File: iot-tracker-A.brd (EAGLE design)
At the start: 25.4 x 21.3 mm, 23 parts, among them U1 ESP-WROOM-02, U2 TPL5111DDCR, U3 MCP1640T-I_CHY

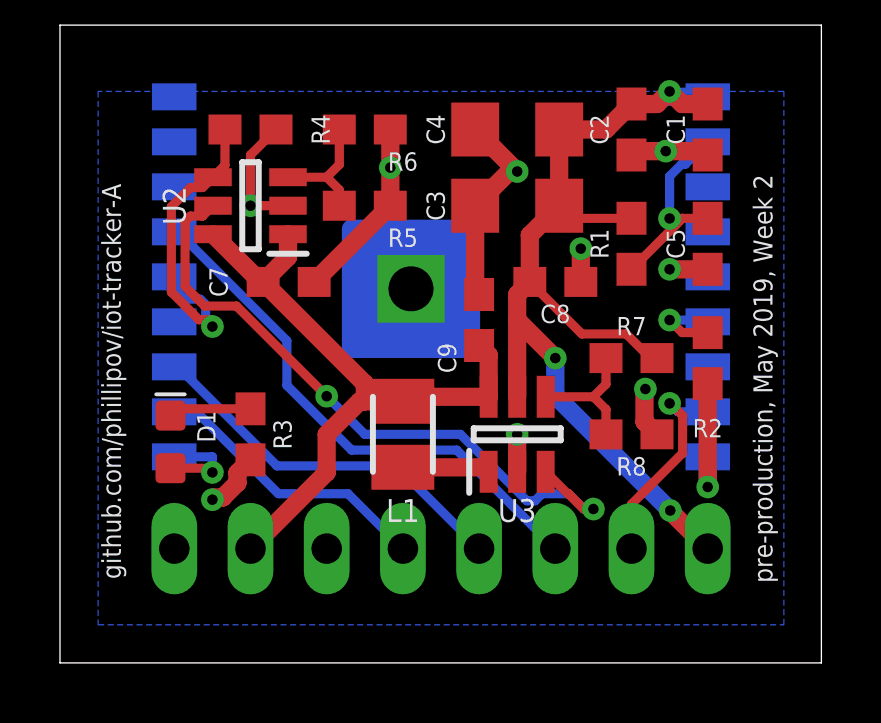
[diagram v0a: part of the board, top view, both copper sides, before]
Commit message: Moved pin headers to top layer and changed silkscreen fonts to vector
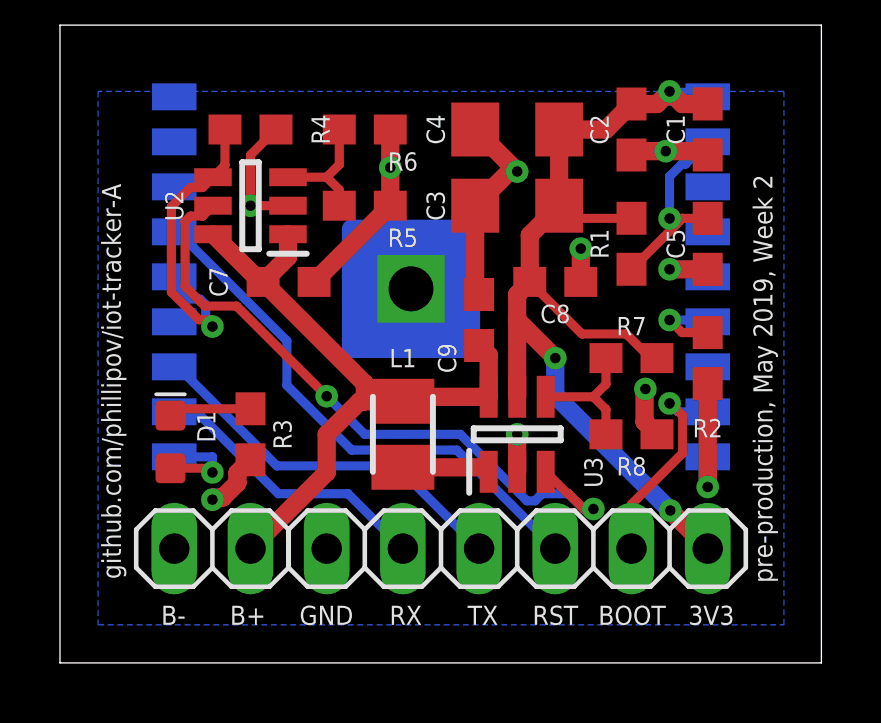
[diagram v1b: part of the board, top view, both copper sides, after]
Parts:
- flipped JP1 to the top, turned to 180 degrees
- flipped JP2 to the top, turned to 180 degrees
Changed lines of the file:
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@@
 <wire x1="25.38" y1="21.26" x2="0" y2="21.26" width="0" layer="20"/>
 <wire x1="0" y1="21.26" x2="0" y2="0" width="0" layer="20"/>
-<text x="6.731" y="1.27" size="0.635" layer="22" font="vector" rot="MR0">B+</text>
-<text x="4.064" y="1.27" size="0.635" layer="22" font="vector" rot="MR0">B-</text>
-<text x="9.652" y="1.27" size="0.635" layer="22" font="vector" rot="MR0">GND</text>
-<text x="14.478" y="1.27" size="0.635" layer="22" font="vector" rot="MR0">TX</text>
-<text x="11.938" y="1.27" size="0.635" layer="22" font="vector" rot="MR0">RX</text>
-<text x="17.145" y="1.27" size="0.635" layer="22" font="vector" rot="MR0">RST</text>
-<text x="20.066" y="1.27" size="0.635" layer="22" font="vector" rot="MR0">BOOT</text>
-<text x="22.352" y="1.27" size="0.635" layer="22" font="vector" rot="MR0">3V3</text>
+<text x="6.858" y="1.905" size="0.635" layer="21" font="vector" rot="R180">B+</text>
+<text x="4.191" y="1.905" size="0.635" layer="21" font="vector" rot="R180">B-</text>
+<text x="9.779" y="1.905" size="0.635" layer="21" font="vector" rot="R180">GND</text>
+<text x="14.605" y="1.905" size="0.635" layer="21" font="vector" rot="R180">TX</text>
+<text x="12.065" y="1.905" size="0.635" layer="21" font="vector" rot="R180">RX</text>
+<text x="17.272" y="1.905" size="0.635" layer="21" font="vector" rot="R180">RST</text>
+<text x="20.193" y="1.905" size="0.635" layer="21" font="vector" rot="R180">BOOT</text>
+<text x="22.479" y="1.905" size="0.635" layer="21" font="vector" rot="R180">3V3</text>
 <text x="2.032" y="2.794" size="0.635" layer="21" font="vector" rot="R90">github.com/phillipov/iot-tracker-A</text>
 <text x="23.749" y="2.667" size="0.635" layer="21" font="vector" rot="R90">pre-production, May 2019, Week 2</text>
@@
 <attribute name="MOUSER_PART_NUMBER" value="" x="49.53" y="40.64" size="1.778" layer="27" rot="R90" display="off"/>
 <attribute name="MOUSER_PRICE-STOCK" value="" x="49.53" y="40.64" size="1.778" layer="27" rot="R90" display="off"/>
-<attribute name="NAME" x="11.43" y="5.08" size="0.762" layer="25" rot="R180" align="center"/>
+<attribute name="NAME" x="11.43" y="10.16" size="0.6096" layer="25" font="vector" ratio="20" rot="R180" align="center"/>
 </element>
 <element name="R1" library="SparkFun-Resistors" library_urn="urn:adsk.eagle:library:532" package="0603" package3d_urn="urn:adsk.eagle:package:39650/1" value="10k" x="19.05" y="13.97" smashed="yes" rot="R270">
@@
 <attribute name="MANUFACTURER_PART_NUMBER" value="TPL5111DDCR" x="-13.97" y="45.72" size="1.778" layer="27" rot="R180" display="off"/>
 <attribute name="MOUSER_PART_NUMBER" value="" x="-13.97" y="45.72" size="1.778" layer="27" rot="R180" display="off"/>
-<attribute name="NAME" x="3.81" y="15.24" size="0.762" layer="25" rot="R270" align="center"/>
+<attribute name="NAME" x="3.81" y="15.24" size="0.6096" layer="25" font="vector" ratio="20" rot="R270" align="center"/>
 </element>
 <element name="U3" library="MCP1640T-I_CHY" package="SOT95P270X145-6N" value="MCP1640T-I_CHY" x="15.24" y="7.62" smashed="yes" rot="R90">
@@
 <attribute name="MOUSER_PART_NUMBER" value="579-MCP1640TI/CHY" x="40.64" y="39.37" size="1.778" layer="27" rot="R90" display="off"/>
 <attribute name="MOUSER_PRICE-STOCK" value="https://www.mouser.com/Search/Refine.aspx?Keyword=579-MCP1640TI%2FCHY" x="40.64" y="39.37" size="1.778" layer="27" rot="R90" display="off"/>
-<attribute name="NAME" x="15.24" y="5.08" size="0.762" layer="25" rot="R180" align="center"/>
-</element>
-<element name="JP1" library="pinhead" library_urn="urn:adsk.eagle:library:325" package="1X06" package3d_urn="urn:adsk.eagle:package:22472/2" value="" x="15.24" y="3.81" smashed="yes" rot="MR0">
-<attribute name="VALUE" x="22.86" y="0.635" size="1.27" layer="28" rot="MR0"/>
-</element>
-<element name="JP2" library="pinhead" library_urn="urn:adsk.eagle:library:325" package="1X02" package3d_urn="urn:adsk.eagle:package:22435/2" value="" x="5.08" y="3.81" smashed="yes" rot="MR0">
-<attribute name="VALUE" x="7.62" y="0.635" size="1.27" layer="28" rot="MR0"/>
+<attribute name="NAME" x="17.78" y="6.35" size="0.6096" layer="25" font="vector" ratio="20" rot="R90" align="center"/>
+</element>
+<element name="JP1" library="pinhead" library_urn="urn:adsk.eagle:library:325" package="1X06" package3d_urn="urn:adsk.eagle:package:22472/2" value="" x="15.24" y="3.81" smashed="yes" rot="R180">
+<attribute name="VALUE" x="22.86" y="6.985" size="1.27" layer="27" rot="R180"/>
+</element>
+<element name="JP2" library="pinhead" library_urn="urn:adsk.eagle:library:325" package="1X02" package3d_urn="urn:adsk.eagle:package:22435/2" value="" x="5.08" y="3.81" smashed="yes" rot="R180">
+<attribute name="VALUE" x="7.62" y="6.985" size="1.27" layer="27" rot="R180"/>
 </element>
 </elements>
@@
 <contactref element="U1" pad="11"/>
 <contactref element="JP1" pad="5"/>
-<wire x1="11.43" y1="3.81" x2="9.6012" y2="5.6388" width="0.3048" layer="16"/>
-<wire x1="9.6012" y1="5.6388" x2="7.2812" y2="5.6388" width="0.3048" layer="16"/>
+<wire x1="7.2812" y1="5.6388" x2="9.6012" y2="5.6388" width="0.3048" layer="16"/>
 <wire x1="7.2812" y1="5.6388" x2="4.55" y2="8.37" width="0.3048" layer="16"/>
 <wire x1="4.55" y1="8.37" x2="3.8075" y2="8.37" width="0.3048" layer="16"/>
+<wire x1="9.6012" y1="5.6388" x2="11.43" y2="3.81" width="0.3048" layer="16"/>
 </signal>
 <signal name="TX">
 <contactref element="U1" pad="12"/>
 <contactref element="JP1" pad="4"/>
-<wire x1="13.97" y1="3.81" x2="11.211990625" y2="6.568009375" width="0.3048" layer="16"/>
-<wire x1="11.211990625" y1="6.568009375" x2="7.23305" y2="6.568009375" width="0.3048" layer="16"/>
+<wire x1="7.23305" y1="6.568009375" x2="11.211990625" y2="6.568009375" width="0.3048" layer="16"/>
 <wire x1="7.23305" y1="6.568009375" x2="3.931059375" y2="9.87" width="0.3048" layer="16"/>
 <wire x1="3.931059375" y1="9.87" x2="3.8075" y2="9.87" width="0.3048" layer="16"/>
+<wire x1="11.211990625" y1="6.568009375" x2="13.97" y2="3.81" width="0.3048" layer="16"/>
 </signal>
 <signal name="BOOT">
@@
 <wire x1="20.32" y1="8.6506" x2="20.5458" y2="8.4248" width="0.3048" layer="1"/>
 <wire x1="20.5458" y1="8.4248" x2="20.57625" y2="8.4248" width="0.3048" layer="1"/>
-<wire x1="19.05" y1="5.28895" x2="19.05" y2="3.81" width="0.3048" layer="1"/>
-<wire x1="20.7548" y1="6.99375" x2="19.05" y2="5.28895" width="0.3048" layer="1"/>
+<wire x1="19.05" y1="5.28895" x2="20.7548" y2="6.99375" width="0.3048" layer="1"/>
+<wire x1="19.05" y1="3.81" x2="19.05" y2="5.28895" width="0.3048" layer="1"/>
 </signal>
 <signal name="EN">
@@
 <wire x1="17.3952" y1="10.9648" x2="18.87625" y2="10.9648" width="0.3048" layer="1"/>
 <wire x1="18.87625" y1="10.9648" x2="19.68105" y2="10.16" width="0.3048" layer="1"/>
-<wire x1="21.59" y1="3.81" x2="20.32" y2="5.08" width="0.6096" layer="1"/>
-<wire x1="20.32" y1="5.08" x2="20.3426" y2="5.08" width="0.6096" layer="1"/>
 <via x="20.3426" y="5.08" extent="1-16" drill="0.35"/>
 <wire x1="20.3426" y1="5.08" x2="16.51" y2="8.9126" width="0.6096" layer="16"/>
@@
 <via x="16.51" y="10.16" extent="1-16" drill="0.35"/>
 <wire x1="16.51" y1="10.16" x2="15.24" y2="11.43" width="0.6096" layer="1"/>
+<wire x1="20.3426" y1="5.08" x2="21.59" y2="3.8326" width="0.6096" layer="1"/>
+<wire x1="21.59" y1="3.8326" x2="21.59" y2="3.81" width="0.6096" layer="1"/>
 </signal>
 <signal name="V_BATT">
@@
 <contactref element="U1" pad="15"/>
 <contactref element="JP1" pad="3"/>
-<wire x1="16.51" y1="3.81" x2="13.225996875" y2="7.094003125" width="0.3048" layer="16"/>
 <wire x1="13.225996875" y1="7.094003125" x2="9.720078125" y2="7.094003125" width="0.3048" layer="16"/>
 <wire x1="9.720078125" y1="7.094003125" x2="7.5625" y2="9.25158125" width="0.3048" layer="16"/>
@@
 <wire x1="7.5625" y1="10.738559375" x2="3.931059375" y2="14.37" width="0.3048" layer="16"/>
 <wire x1="3.931059375" y1="14.37" x2="3.8075" y2="14.37" width="0.3048" layer="16"/>
+<wire x1="16.51" y1="3.81" x2="13.225996875" y2="7.094003125" width="0.3048" layer="16"/>
 </signal>
 </signals>

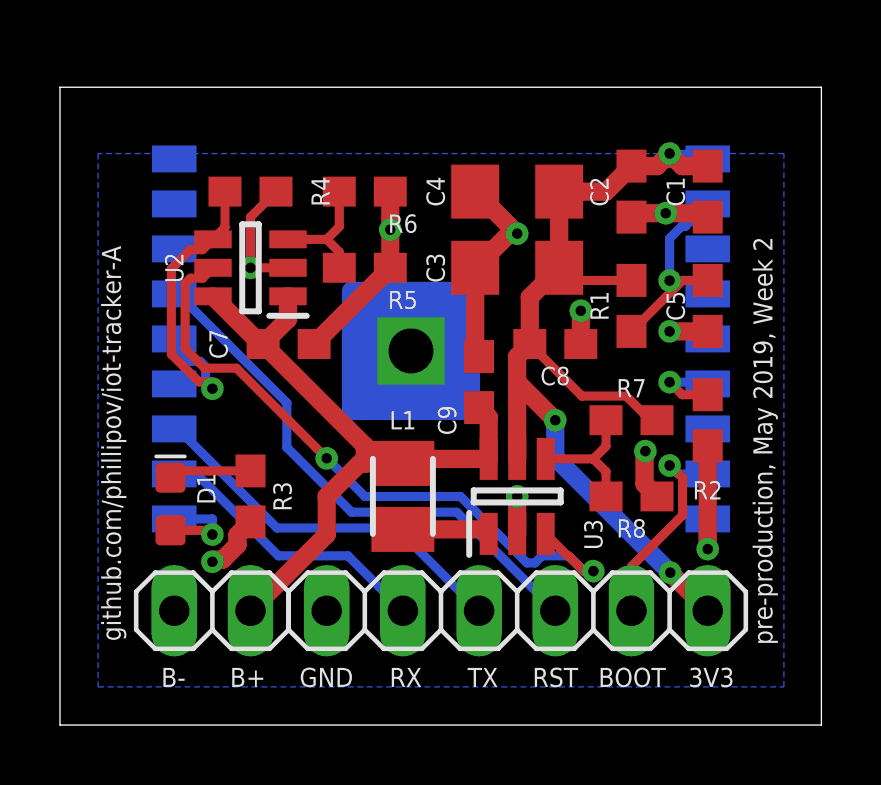
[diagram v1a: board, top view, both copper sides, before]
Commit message: Slightly decreased board size for OSH Park pricing
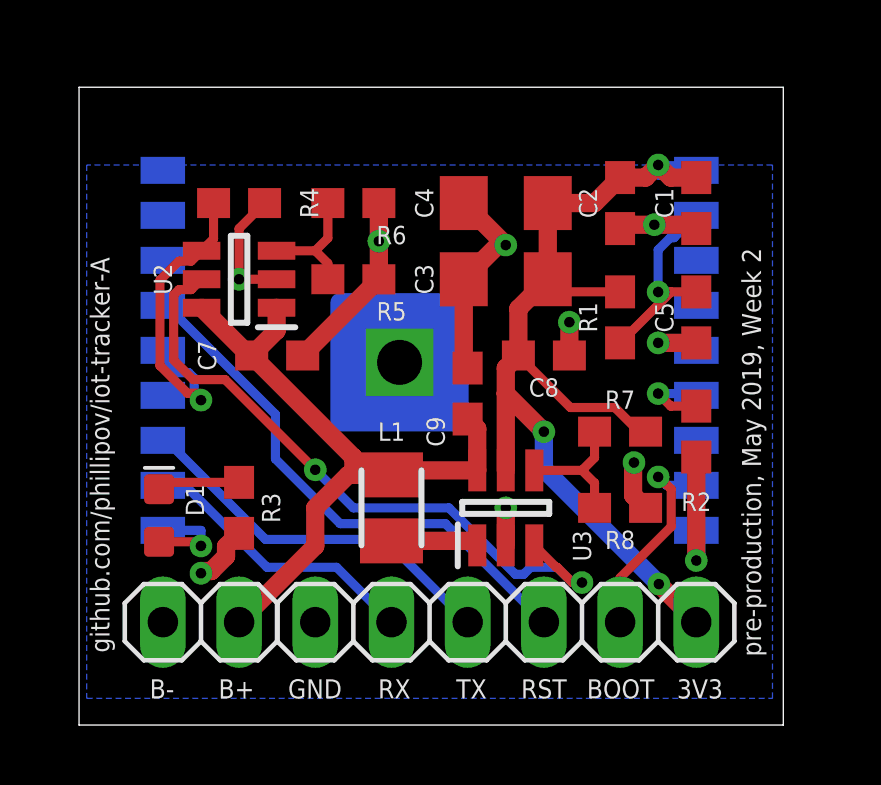
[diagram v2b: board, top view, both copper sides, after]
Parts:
- moved C1 0.54 mm to (21.2, 17.4)
- moved C2 0.54 mm to (18.7, 17.4)
- moved C3 0.54 mm to (14.9, 14.9)
- moved C4 0.54 mm to (14.9, 17.4)
- moved C5 0.54 mm to (21.2, 13.6)
- moved C9 0.54 mm to (13.6, 11.0)
- moved JP1 0.54 mm to (14.9, 3.43)
- moved JP2 0.54 mm to (4.70, 3.43)
- moved L1 0.54 mm to (11.0, 7.24)
- moved R1 0.54 mm to (18.7, 13.6)
- moved R2 0.54 mm to (21.2, 9.78)
- moved R5 0.54 mm to (9.78, 14.9)
- moved R6 0.54 mm to (9.78, 17.4)
- moved R7 0.54 mm to (18.7, 9.78)
- moved R8 0.54 mm to (18.7, 7.24)
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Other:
- board size 25.4 x 21.3 mm -> 23.5 x 21.3 mm

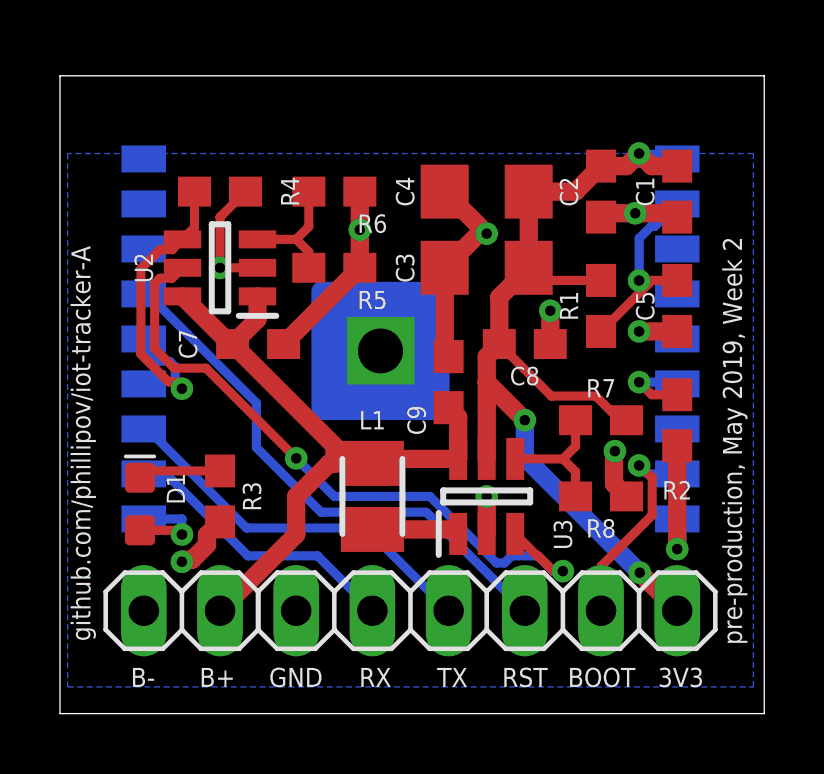
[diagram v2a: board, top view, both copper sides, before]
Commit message: Reorganized component placement and consolidated headers into a single 1x8 part
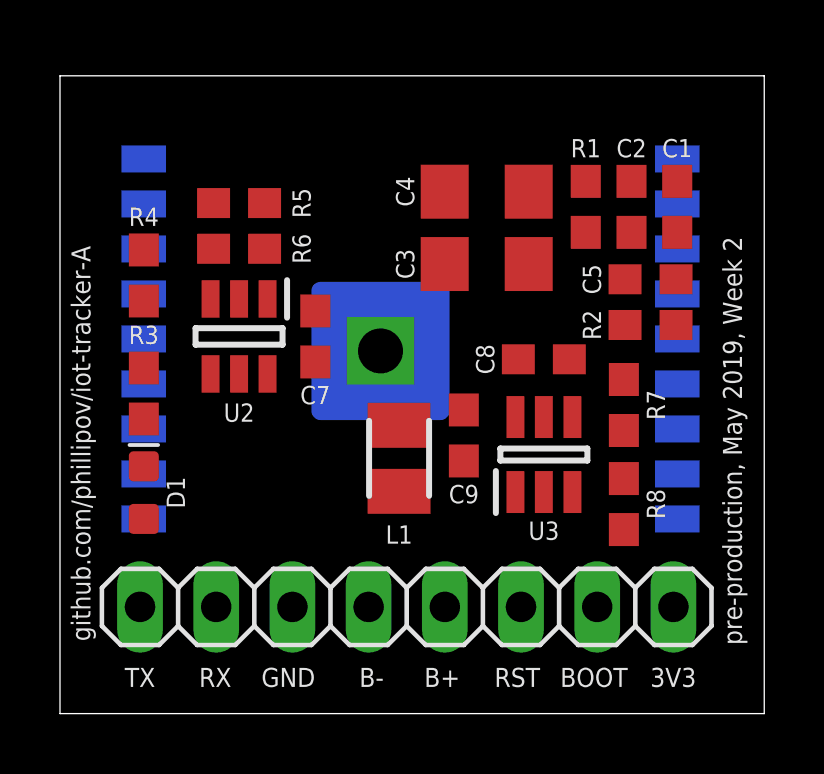
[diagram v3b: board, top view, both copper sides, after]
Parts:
- removed JP2: (no value), pinhead:1X02
- JP1: device pinhead:1X06 -> pinhead:1X08
- moved R3 4.27 mm to (3.43, 10.7), turned to 270 degrees
- moved R5 3.84 mm to (6.60, 17.0)
- moved R4 3.78 mm to (3.43, 14.6), turned to 90 degrees
- moved R6 3.70 mm to (6.60, 15.5)
- moved R1 3.34 mm to (18.2, 16.9)
- moved R2 3.30 mm to (20.3, 13.0), turned to 180 degrees
- moved JP1 2.67 mm to (12.2, 3.56)
- moved U2 2.37 mm to (6.60, 12.6), turned to 270 degrees
- moved U3 2.36 mm to (16.8, 8.64)
- moved C7 1.92 mm to (9.14, 12.6), turned to 270 degrees
- moved C9 1.85 mm to (14.1, 9.27), turned to 90 degrees
- moved L1 1.55 mm to (11.9, 8.51)
- moved C5 1.26 mm to (20.3, 14.5), turned to 0 degrees
- moved C2 1.14 mm to (19.7, 16.9)
- moved R7 0.92 mm to (19.4, 10.3), turned to 270 degrees
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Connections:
- net GND: now also JP1.5; no longer JP2.2
- net RX: now also JP1.7; no longer JP1.5
- net TX: now also JP1.8; no longer JP1.4
- net V_BATT: now also JP1.4; no longer JP2.1
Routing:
- net 3.3V: track 34.7 -> 0.00 mm, vias 3 -> 0
- net GND: track 31.7 -> 0.00 mm, vias 10 -> 0
- net DRVN: track 22.3 -> 0.00 mm, vias 2 -> 0
- net V_BATT: track 22.3 -> 0.00 mm
- net RST: track 17.9 -> 0.00 mm
- net TX: track 12.7 -> 0.00 mm
- net DONE: track 10.9 -> 0.00 mm, vias 1 -> 0
- net RX: track 9.51 -> 0.00 mm
- net BOOT: track 7.13 -> 0.00 mm, vias 1 -> 0
- net EN: track 6.83 -> 0.00 mm, vias 1 -> 0
- net VFB: track 4.48 -> 0.00 mm
- net DELAY: track 4.18 -> 0.00 mm
- net IO4_LED: track 3.25 -> 0.00 mm, vias 1 -> 0
- net SW: track 2.92 -> 0.00 mm
- net LED_GND: track 2.76 -> 0.00 mm
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- removed copper zone on layer 16, net GND

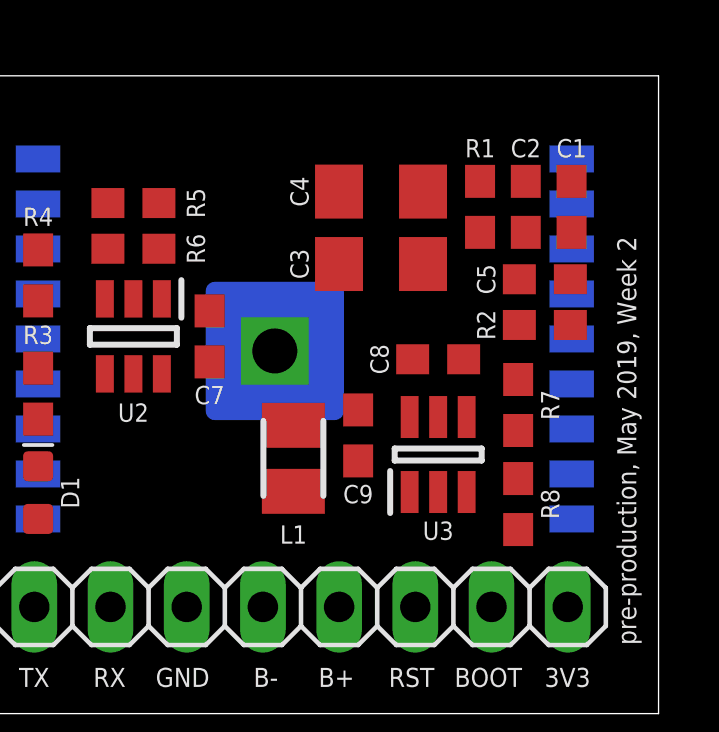
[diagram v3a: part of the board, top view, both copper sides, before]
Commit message: Adjusted placement and defined net classes
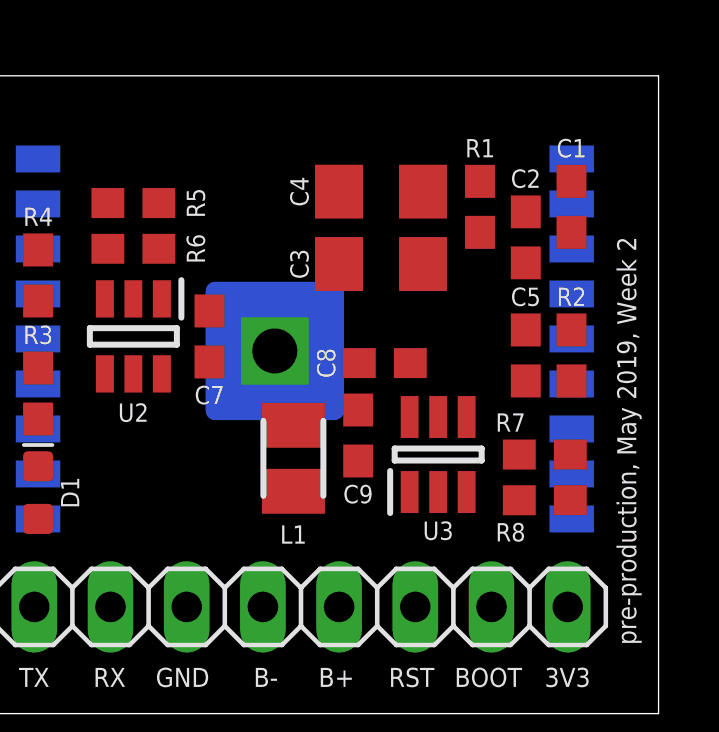
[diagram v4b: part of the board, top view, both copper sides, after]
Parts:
- moved C5 2.62 mm to (19.7, 11.9), turned to 90 degrees
- moved R7 1.88 mm to (20.3, 8.64), turned to 180 degrees
- moved C8 1.78 mm to (15.0, 11.7)
- moved R2 1.35 mm to (21.2, 11.9), turned to 270 degrees
- moved C2 1.02 mm to (19.7, 15.9)
- moved R8 0.90 mm to (20.3, 7.11), turned to 0 degrees

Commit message: Unleashed the autorouter
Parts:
- moved C2 1.83 mm to (21.2, 16.9)
- moved C1 1.65 mm to (19.7, 16.3)
- moved C8 0.18 mm to (14.9, 11.8)
- moved L1 0.18 mm to (11.8, 8.64)
- moved R7 0.18 mm to (20.2, 8.76)
- moved U3 0.18 mm to (16.6, 8.76)
- moved R8 0.18 mm to (20.2, 7.24)
- moved C9 0.18 mm to (14.0, 9.40)
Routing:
- net 3.3V: track 0.00 -> 50.8 mm, vias 0 -> 3
- net GND: track 0.00 -> 40.4 mm, vias 0 -> 2
- net V_BATT: track 0.00 -> 25.7 mm, vias 0 -> 3
- net RST: track 0.00 -> 25.1 mm
- net DONE: track 0.00 -> 21.0 mm, vias 0 -> 2
- net IO15: track 0.00 -> 16.5 mm, vias 0 -> 1
- net DRVN: track 0.00 -> 14.9 mm
- net BOOT: track 0.00 -> 13.3 mm
- net EN: track 0.00 -> 8.15 mm, vias 0 -> 1
- net TX: track 0.00 -> 7.95 mm
- net RX: track 0.00 -> 6.20 mm
- net SW: track 0.00 -> 3.96 mm
- net VFB: track 0.00 -> 3.83 mm
- net DELAY: track 0.00 -> 3.28 mm
- net IO4_LED: track 0.00 -> 2.64 mm, vias 0 -> 1
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- added copper zone on layer 16, net GND
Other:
- board size 23.5 x 21.3 mm -> 23.5 x 20 mm
